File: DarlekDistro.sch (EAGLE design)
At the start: 36 parts, among them J1 POWERPOLE_POWER10AWG, J10 FUSEATC, J11 POWERPOLE_POWER10AWG, J12 FUSEATC, J2 FUSEATC, J3 POWERPOLE_POWER10AWG, J4 FUSEATC, J5 POWERPOLE_POWER10AWG, J6 FUSEATC, J7 POWERPOLE_POWER10AWG, J8 FUSEATC, J9 POWERPOLE_POWER10AWG

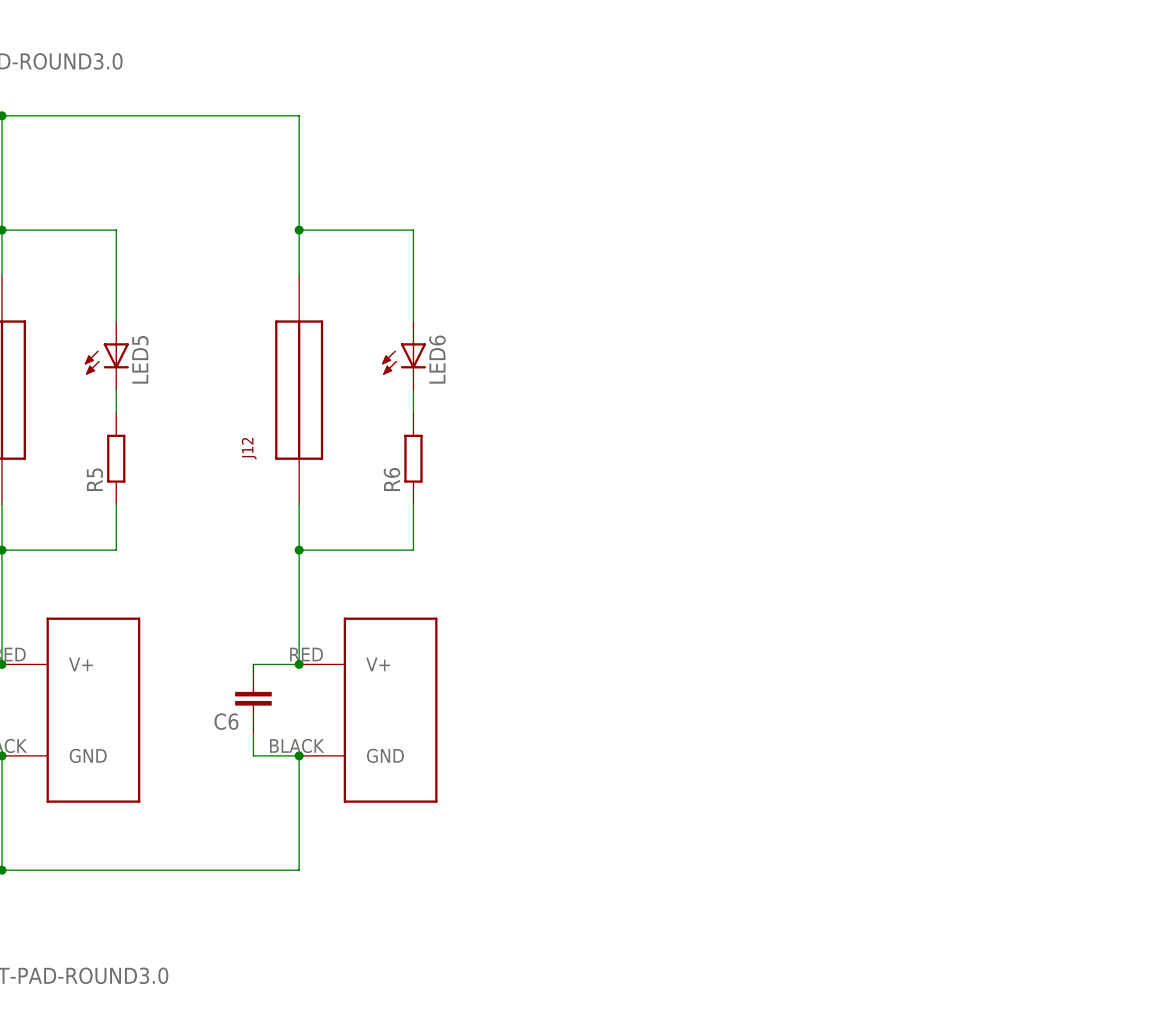
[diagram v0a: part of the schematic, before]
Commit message: Added 5v reg and connectors
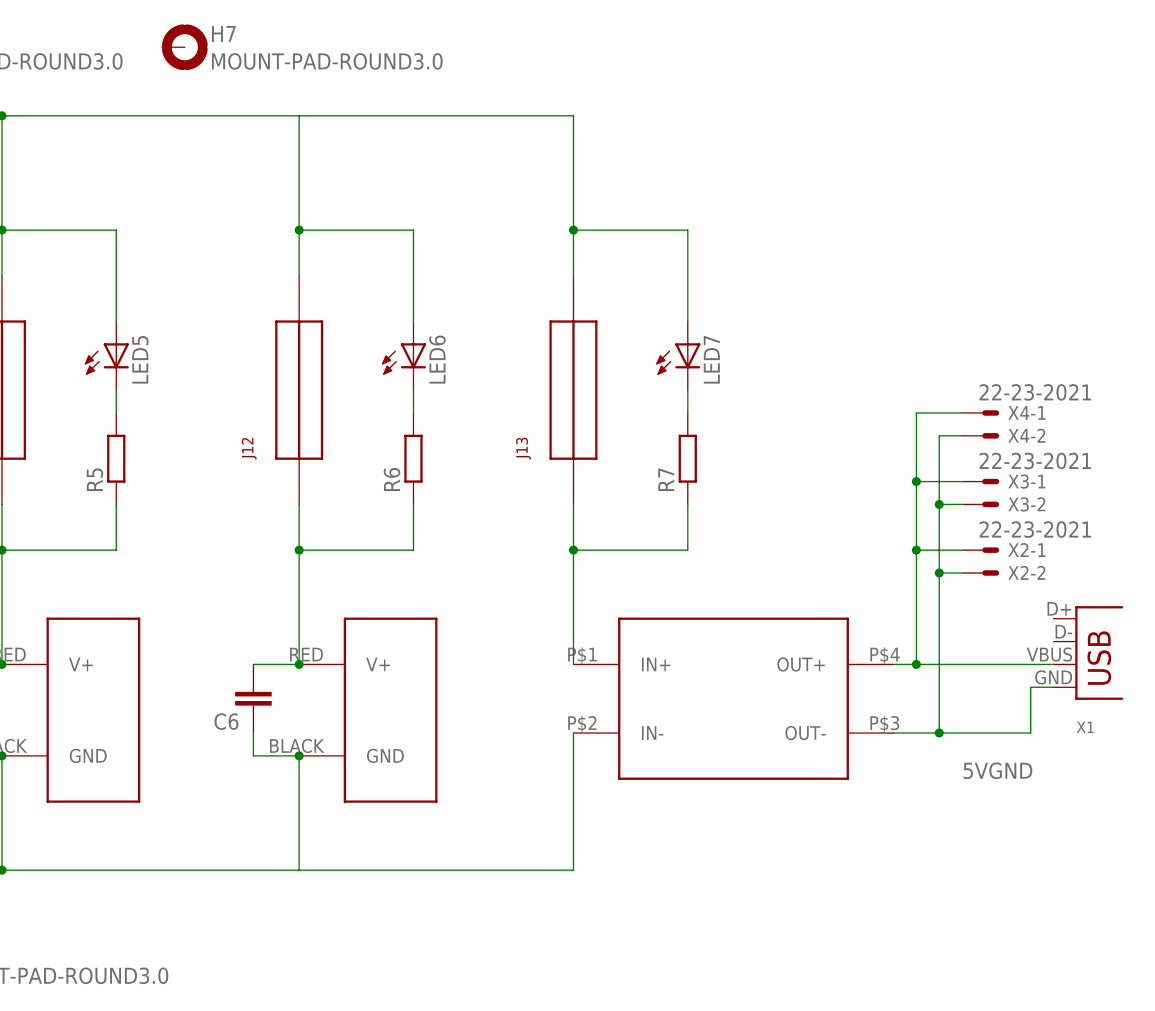
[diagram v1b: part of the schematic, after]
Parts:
- added H7: MOUNT-PAD-ROUND3.0, holes:MOUNT-PAD-ROUND3.0
- added J13: FUSEATC, powerpoles:FUSEATC
- added LED7: (no value), adafruit:LED3MM
- added R7: (no value), rcl:R-EU_0204/7
- added U$1: DSN2596_REG, DarlekParts:DSN2596_REG
- added X1: (no value), con-usb-3:USB-A-H
- added X2, X3, X4: 22-23-2021, con-molex:22-23-2021
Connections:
- new net 5VGND: U$1.OUT-, X1.GND, X2-2.S, X3-2.S, X4-2.S
- new net N$7: LED7.C, R7.2
- new net N$8: U$1.OUT+, X1.VBUS, X2-1.S, X3-1.S, X4-1.S
- new net PPV7: J13.P$1, R7.1, U$1.IN+
- net GND: now also U$1.IN-
- net VCC: now also J13.P$2, LED7.A
